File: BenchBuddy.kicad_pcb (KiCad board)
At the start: 4 copper layers, 165.1 x 63.5 mm, 57 parts, among them K1 1461069-5, P1 24 Pin MiniFit JR, P2 CONN_3X2, P3 CONN_2, P4 12 Pin Terminal Block, P5 3 Pin TB, Q1 2N3904, U1 LTV-816S, U2 MCP3901, U3 LMT84, U4 OPA4170

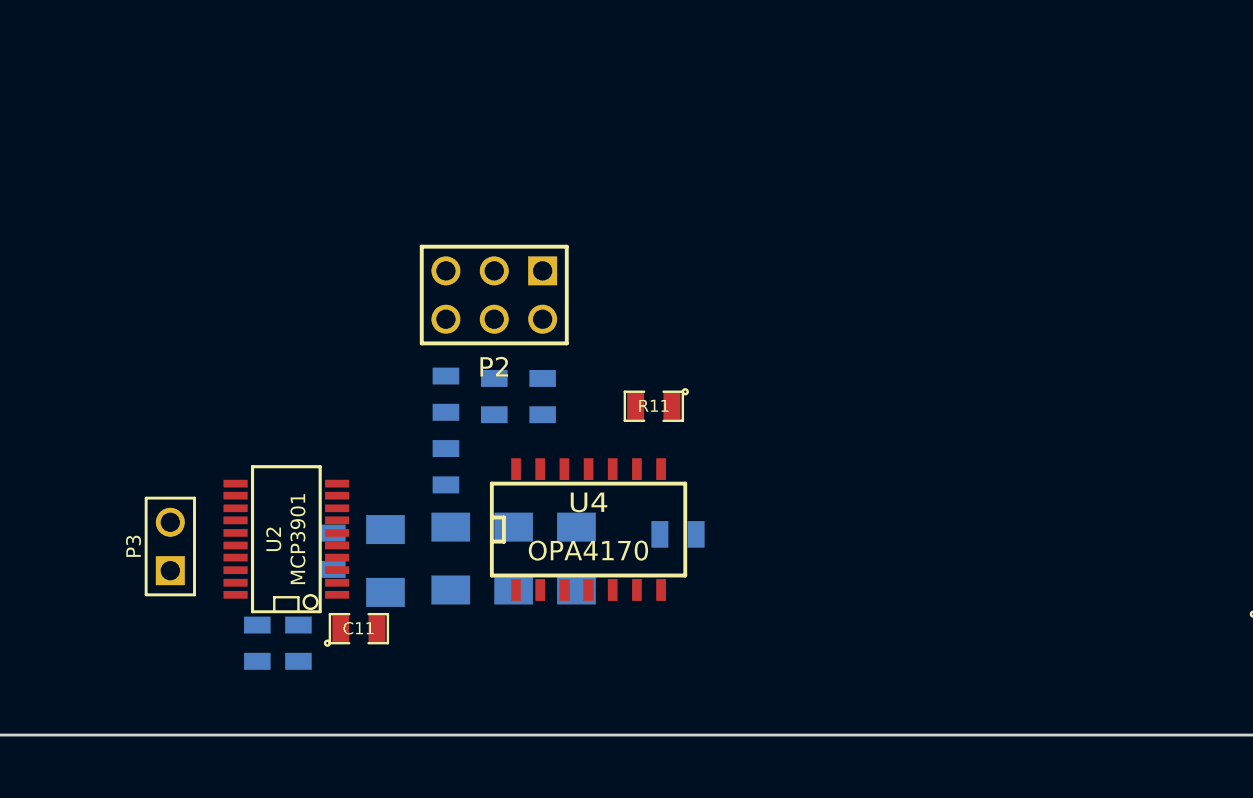
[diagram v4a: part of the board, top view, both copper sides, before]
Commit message: Placing Current Module Components
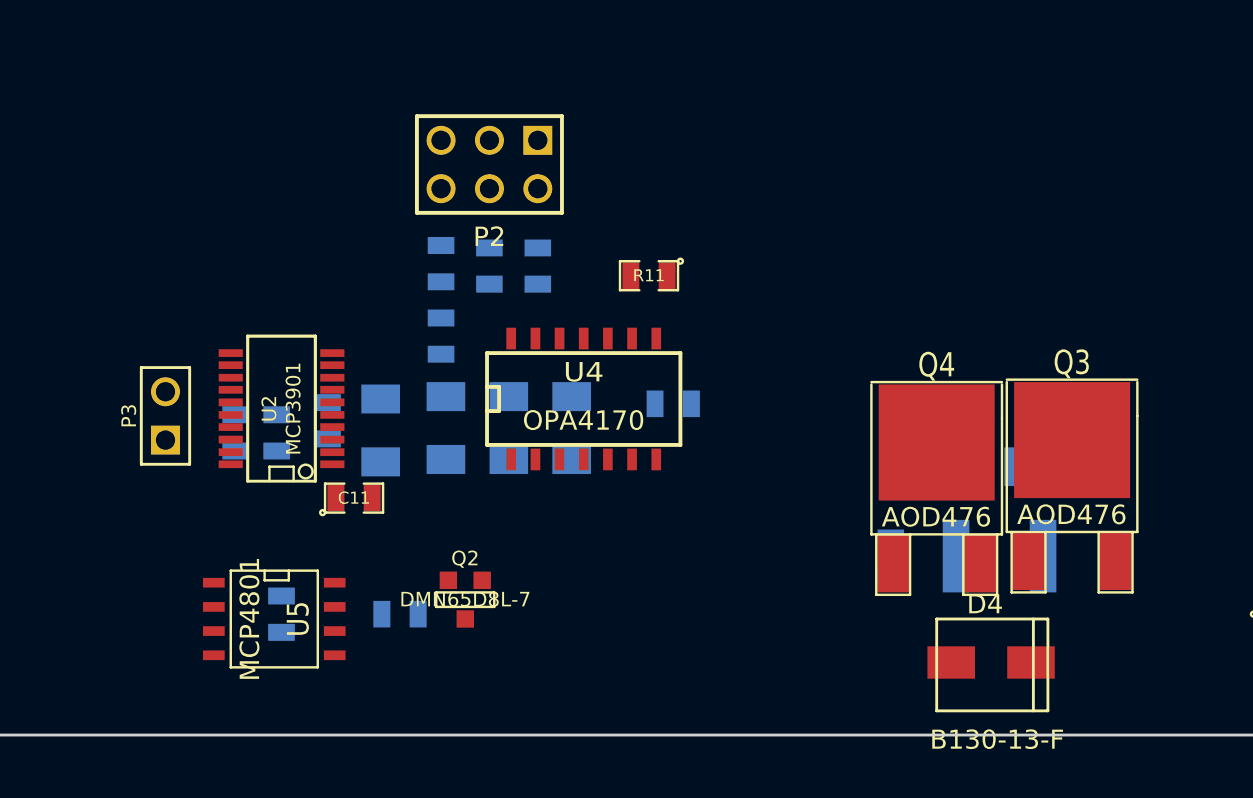
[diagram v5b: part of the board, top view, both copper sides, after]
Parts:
- added C12: C, SM0805, B.Cu at (231.0, 152.9)
- added C13: C, SM0805, B.Cu at (263.0, 149.9)
- added D4: B130-13-F, SMA, F.Cu at (266.2, 155.4)
- added Q2: DMN65D8L-7, SOT23GDS, F.Cu at (240.7, 152.1)
- added Q3: AOD476, DPAK2, F.Cu at (272.5, 150.1)
- added Q4: AOD476, DPAK2, F.Cu at (265.4, 150.2)
- added R15: R, SM0805, B.Cu at (237.2, 152.9)
- added R16: R, SM1206, B.Cu at (268.1, 145.2)
- added TH5: MINISMDC050F-2, SM1812, B.Cu at (268.7, 149.9)
- added U5: MCP4801, SO8N, F.Cu at (230.6, 153.2)
- moved C7 11.1 mm to (228.6, 143.4)
- moved C8 11.1 mm to (230.8, 143.4)
- moved C1 6.86 mm to (233.4, 142.7)
- moved C10 6.86 mm to (251.6, 141.9)
- moved R10 6.86 mm to (246.3, 143.1)
- moved R12 6.86 mm to (244.5, 134.6)
- moved R9 6.86 mm to (243.0, 143.1)
- moved P2 6.86 mm to (241.9, 129.3)
- moved P3 6.86 mm to (224.9, 142.5)
- moved R11 6.86 mm to (250.3, 135.1)
- moved R13 6.86 mm to (239.4, 138.3)
- moved R44 6.86 mm to (239.4, 134.5)
- moved R45 6.86 mm to (241.9, 134.6)
- moved R7 6.86 mm to (239.6, 143.1)
- moved R8 6.86 mm to (236.2, 143.3)
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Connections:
- net /Arduino/ADC_CS_N renamed /Arduino/~ADC_CS
- ARD1 pad 13: (no net) -> N-0000060
- ARD1 pad 14: (no net) -> N-0000059
- P4 pad 10: /Arduino/CURR_MEAS -> /Fan/TACH_IN
- R33 pad 2: /Fan/CURR_MEAS -> /Fan/TACH_IN
- U4 pad 6: /Fan/CURR_MEAS -> /Arduino/CURR_MEAS

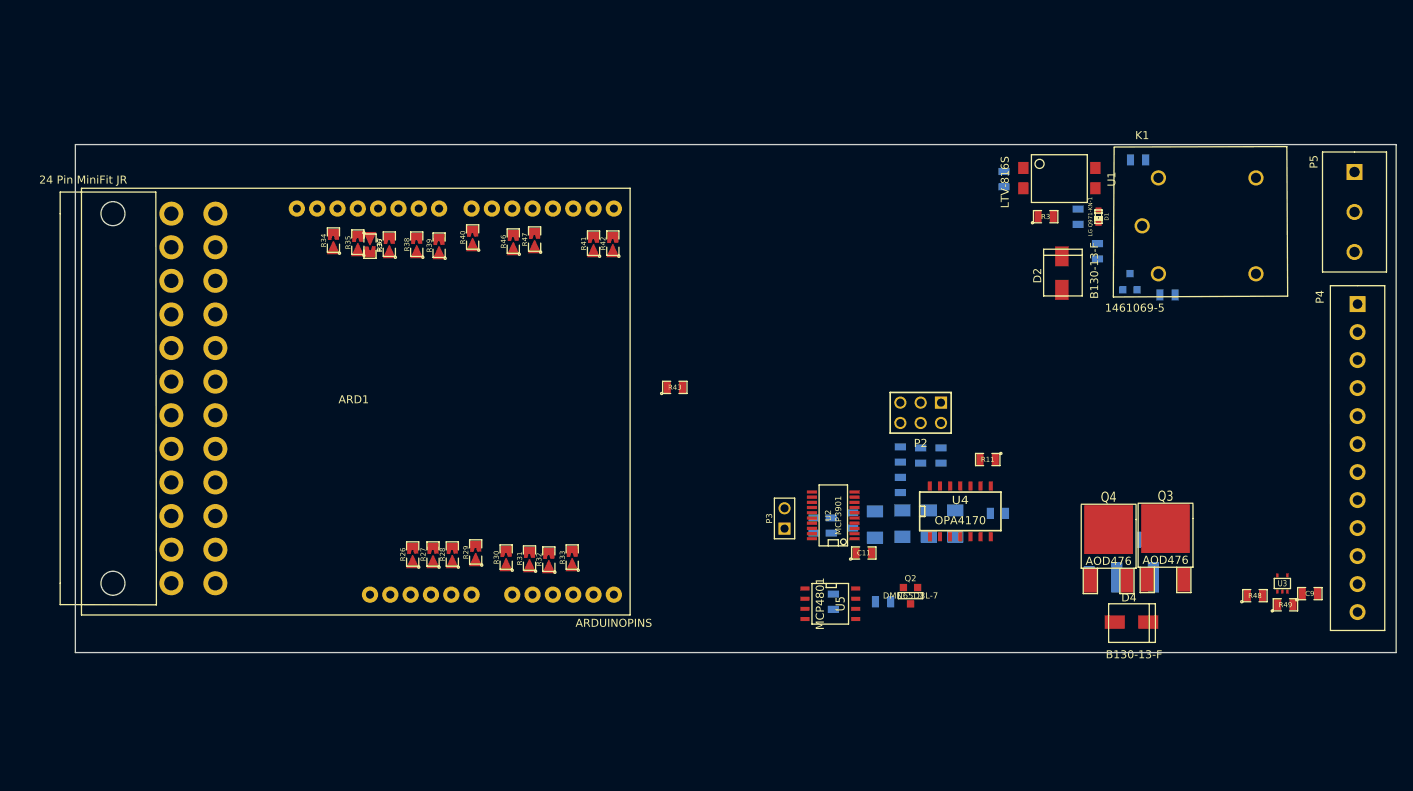
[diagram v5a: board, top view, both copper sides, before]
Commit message: Placing the Filter Module
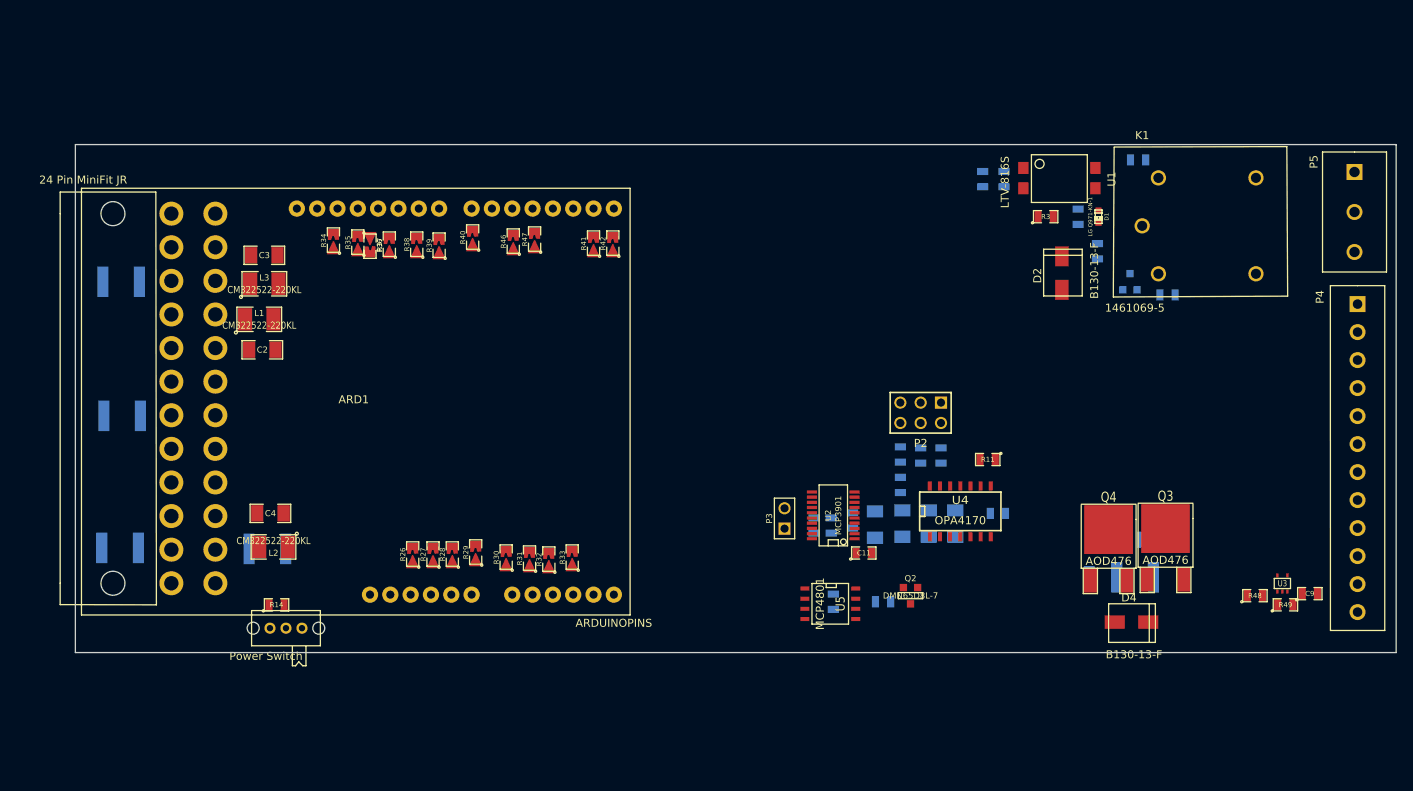
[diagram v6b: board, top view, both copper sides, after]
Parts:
- added C2: C, SM1206, F.Cu at (159.6, 121.4)
- added C3: C, SM1206, F.Cu at (159.9, 109.6)
- added C4: C, SM1206, F.Cu at (160.7, 141.9)
- added L1: CM322522-220KL, SM1210L, F.Cu at (159.3, 117.6)
- added L2: CM322522-220KL, SM1210L, F.Cu at (161.0, 146.1)
- added L3: CM322522-220KL, SM1210L, F.Cu at (159.9, 113.2)
- added R14: R, SM0805, F.Cu at (161.4, 153.3)
- added SW1: Power Switch, BB_switch, F.Cu at (158.5, 156.2)
- added TH1: MINISMDC050F-2, SM1812, B.Cu at (141.9, 146.2)
- added TH2: MINISMDC050F-2, SM1812, B.Cu at (142.1, 129.7)
- added TH3: MINISMDC050F-2, SM1812, B.Cu at (142.0, 112.9)
- added TH4: MINISMDC050F-2, SM1812, B.Cu at (160.3, 146.3)
- R43: moved to B.Cu
- moved R43 46.5 mm to (249.7, 100.1), turned to 270 degrees

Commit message: Placing the Power Modify Module
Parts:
- added C14: C, SM0805, B.Cu at (186.4, 137.4)
- added C15: C, SM0805, B.Cu at (187.6, 123.9)
- added C16: C, SM0805, B.Cu at (221.8, 110.8)
- added C17: C, SM0805, B.Cu at (224.3, 149.0)
- added C18: C, SM0805, B.Cu at (221.1, 105.0)
- added C19: C, SM0805, B.Cu at (228.1, 151.7)
- added C20: C, SM0805, B.Cu at (193.2, 135.3)
- added C21: C, SM0805, B.Cu at (193.7, 125.6)
- added C22: C, SM0805, B.Cu at (221.7, 152.3)
- added C23: C, SM0805, B.Cu at (199.3, 120.9)
- added C24: C, SM0805, B.Cu at (187.6, 134.7)
- added C25: C, SM0805, B.Cu at (199.6, 123.2)
- added D10: MMBD914-7-F, SOT23-DIODE, F.Cu at (196.7, 135.1)
- added D11: MMBD914-7-F, SOT23-DIODE, F.Cu at (223.1, 106.3)
- added D12: MMBD914-7-F, SOT23-DIODE, F.Cu at (197.3, 118.1)
- added D3: MMBD914-7-F, SOT23-DIODE, F.Cu at (214.8, 105.5)
- added D6: MMBD914-7-F, SOT23-DIODE, F.Cu at (216.6, 157.3)
- added D7: MMBD914-7-F, SOT23-DIODE, F.Cu at (193.2, 120.1)
- added D8: MMBD914-7-F, SOT23-DIODE, F.Cu at (215.4, 150.6)
- added D9: MMBD914-7-F, SOT23-DIODE, F.Cu at (199.5, 135.7)
- added R18: 715, SM0805, B.Cu at (222.8, 107.9)
- added R19: 5K, EVUE3K, F.Cu at (233.7, 102.4)
- added R20: 5K, EVUE3K, F.Cu at (238.4, 151.8)
- added R21: 715, SM0805, B.Cu at (227.7, 154.5)
- added R22: R, SM0805, B.Cu at (221.6, 145.8)
- added R23: R, SM0805, B.Cu at (195.2, 133.1)
- added R24: R, SM0805, B.Cu at (199.5, 125.7)
- added R25: R, SM0805, B.Cu at (218.9, 111.9)
- added R50: R, SM0805-blob, F.Cu at (195.9, 107.8)
- added R51: R, SM0805-blob, F.Cu at (198.3, 108.1)
- added R52: R, SM0805, B.Cu at (189.0, 126.0)
- added R53: R, SM0805, B.Cu at (187.7, 121.5)
- added R54: R, SM0805, B.Cu at (191.2, 136.8)
- added R55: R, SM0805, B.Cu at (190.3, 140.2)
- added U11: LM317, TO220, F.Cu at (226.4, 153.6)
- added U6: LM337T, TO220, F.Cu at (221.5, 107.9)
- added U8: LM337T, TO220, F.Cu at (180.2, 123.3)
- added U9: LM317, TO220, F.Cu at (180.3, 136.4)
- moved C1 15.4 mm to (248.8, 144.3)
- moved C10 15.4 mm to (267.0, 143.4)
- moved C7 15.4 mm to (244.0, 144.9)
- moved C8 15.4 mm to (246.1, 144.9)
- moved P2 15.4 mm to (257.3, 130.8)
- moved R10 15.4 mm to (261.6, 144.7)
- moved R11 15.4 mm to (265.7, 136.7)
- moved R15 15.4 mm to (252.6, 154.4)
- moved R45 15.4 mm to (257.3, 136.1)
- moved C11 15.4 mm to (250.2, 148.3)
- moved C12 15.4 mm to (246.4, 154.4)
- moved P3 15.4 mm to (240.3, 144.0)
- moved Q2 15.4 mm to (256.0, 153.7)
- moved R12 15.4 mm to (259.8, 136.1)
- moved R13 15.4 mm to (254.8, 139.8)
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
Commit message: Placing the LED Module
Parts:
- added C5: 1U, SM0805, B.Cu at (223.0, 128.5)
- added C6: 1U, SM0805, B.Cu at (225.6, 128.3)
- added D5: B0540WS-7, SOD-323, F.Cu at (221.7, 129.9)
- added L4: 22u, NR4012, F.Cu at (230.2, 127.1)
- added R17: 15, SM0805, B.Cu at (227.8, 128.2)
- added U7: AP5726, SOT23_6, F.Cu at (225.3, 128.6)
